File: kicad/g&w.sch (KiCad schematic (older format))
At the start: 181 parts, among them IC1 audio, IC2 MX25U8035F, IC3 vreg, IC4 pmic, IC5 BQ24072RGT_, J1 speaker, J2 SWD PORT, J3 DISPLAY1, J4 DISPLAY2, J5 Battery, J6 USB-C, Q1 PMBT3904, Q2 PMBT3904, Q3 PMBT3904, Q4 SSM6J412TU, Y1 H01717

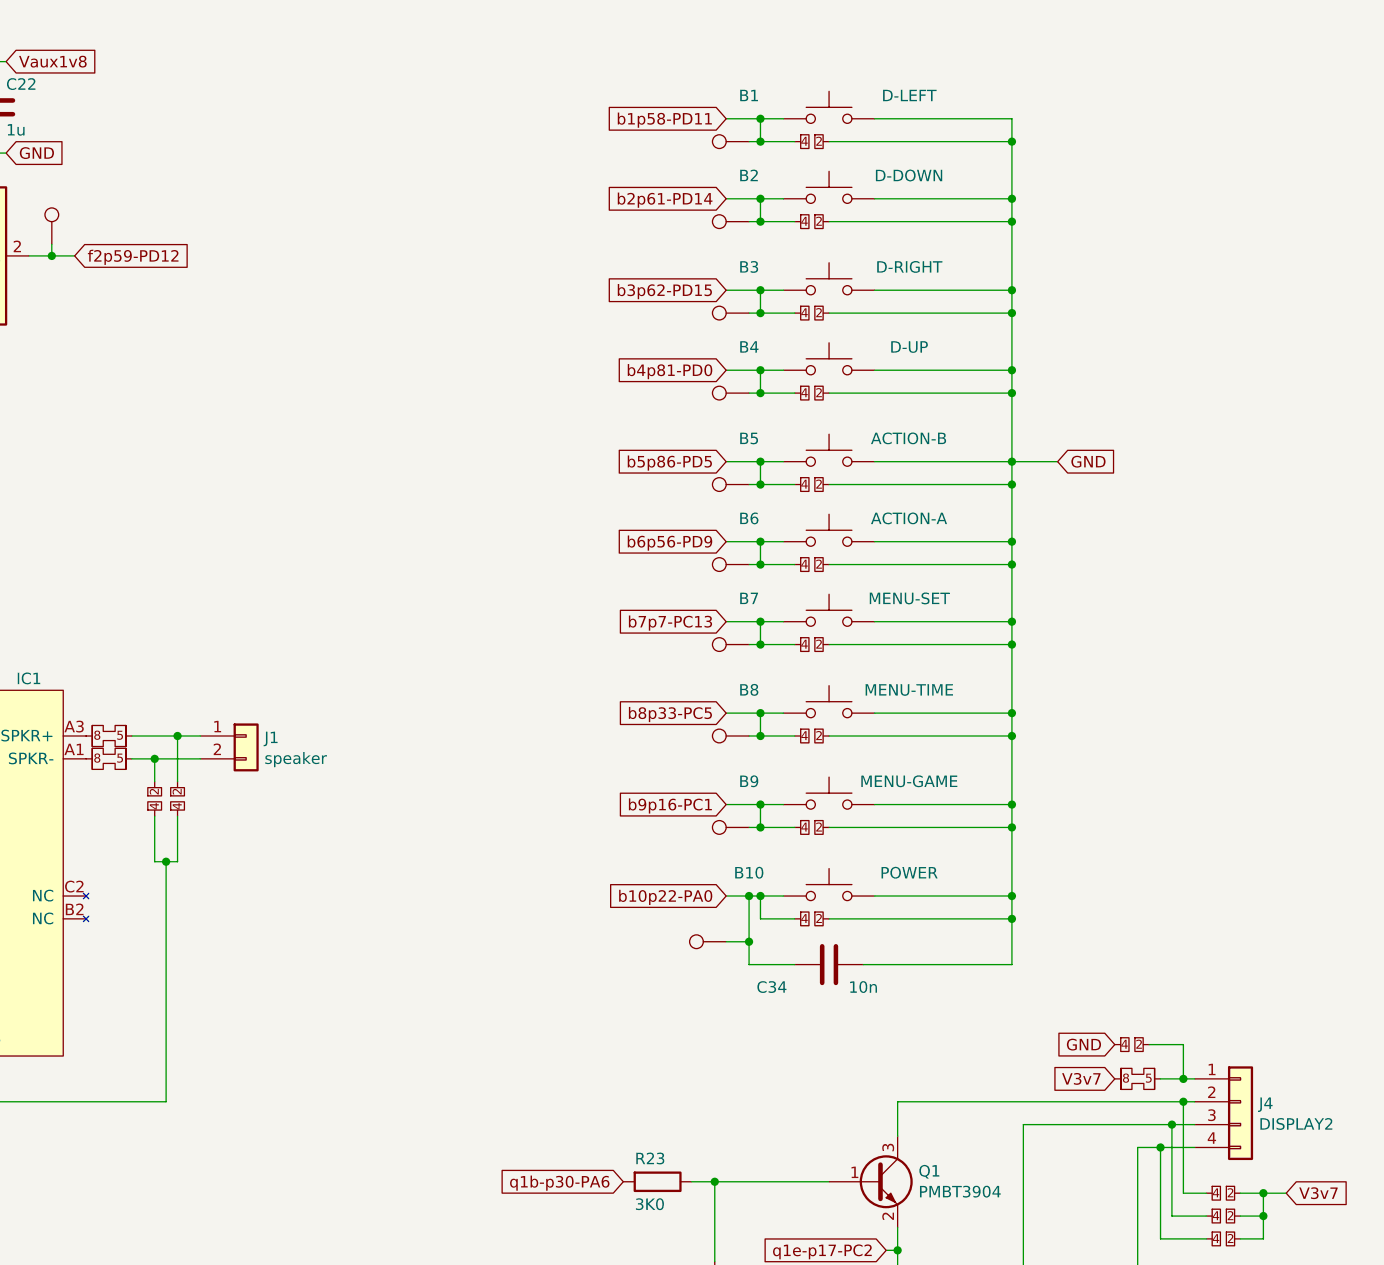
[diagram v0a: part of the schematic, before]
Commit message: kicad board outline
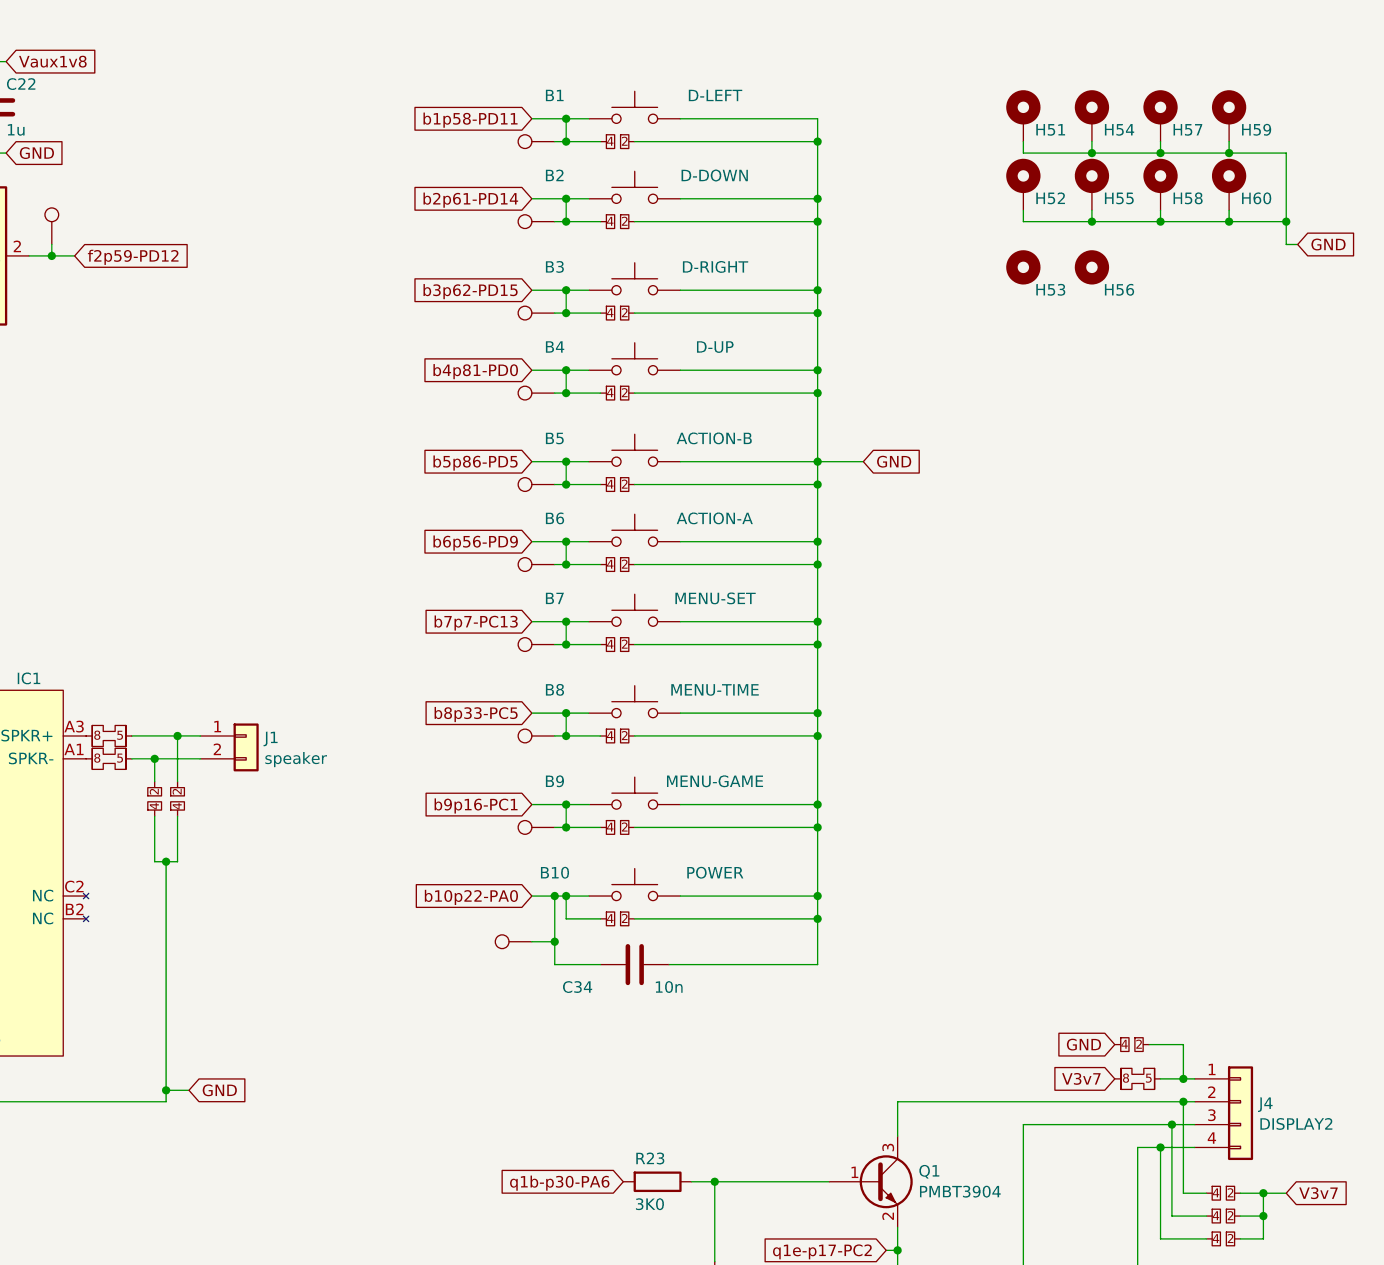
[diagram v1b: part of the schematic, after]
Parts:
- added H51, H52, H54, H55, H57, H58, H59, H60: MountingHole_Pad, gnw:MountingHole_2.0mm, symbol Mechanical:MountingHole_Pad
- added H53: MountingHole, gnw:MountingSlot_NC_1.3x2.2mm, symbol Mechanical:MountingHole
- added H56: MountingHole, gnw:MountingHole_NC_1.5mm, symbol Mechanical:MountingHole
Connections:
- net GND: now also IC1.A2 (GND), IC1.C3 (GND), JP78.1, JP79.1, JP86.1, JP87.1, R1.1, R2.2, R3.1, R4.2, H51.1, H52.1, H54.1, H55.1, H57.1, H58.1, H59.1, H60.1
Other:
- moved on the sheet: B1, B10, B2, B3, B4, B5, B6, B7, B8, B9, C34

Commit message: tweak footprints, setup design rules for 4 layers at common proto board house and refine board outline
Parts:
- TP51, TP52, TP53, TP54, TP55, TP56, TP57, TP58, TP59, TP60, TP61, TP62, TP63, TP64, TP65, TP66, TP67, TP68, TP69, TP70, TP71, TP72, TP73, TP74, TP75, TP76, TP77, TP78, TP79, TP80: footprint TestPoint:TestPoint_Pad_D1.0mm -> gnw:gnw-TestPoint_Pad_D1.0mm
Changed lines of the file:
@@
 F 0 "TP70" H 11158 7072 50  0001 L CNN
 F 1 "TestPoint" H 11158 7027 50  0001 L CNN
-F 2 "TestPoint:TestPoint_Pad_D1.0mm" H 11300 7000 50  0001 C CNN
+F 2 "gnw:gnw-TestPoint_Pad_D1.0mm" H 11300 7000 50  0001 C CNN
 F 3 "~" H 11300 7000 50  0001 C CNN
 	1    11100 7000
@@
 F 0 "TP68" H 9908 7722 50  0001 L CNN
 F 1 "TestPoint" H 9908 7677 50  0001 L CNN
-F 2 "TestPoint:TestPoint_Pad_D1.0mm" H 10050 7650 50  0001 C CNN
+F 2 "gnw:gnw-TestPoint_Pad_D1.0mm" H 10050 7650 50  0001 C CNN
 F 3 "~" H 10050 7650 50  0001 C CNN
 	1    9850 7650
@@
 F 0 "TP67" H 10158 1572 50  0001 L CNN
 F 1 "TestPoint" H 10158 1527 50  0001 L CNN
-F 2 "TestPoint:TestPoint_Pad_D1.0mm" H 10300 1500 50  0001 C CNN
+F 2 "gnw:gnw-TestPoint_Pad_D1.0mm" H 10300 1500 50  0001 C CNN
 F 3 "~" H 10300 1500 50  0001 C CNN
 	1    10100 1500
@@
 F 0 "TP63" H 8958 1472 50  0001 L CNN
 F 1 "TestPoint" H 8958 1427 50  0001 L CNN
-F 2 "TestPoint:TestPoint_Pad_D1.0mm" H 9100 1400 50  0001 C CNN
+F 2 "gnw:gnw-TestPoint_Pad_D1.0mm" H 9100 1400 50  0001 C CNN
 F 3 "~" H 9100 1400 50  0001 C CNN
 	1    8900 1400
@@
 F 0 "TP64" H 8958 1572 50  0001 L CNN
 F 1 "TestPoint" H 8958 1527 50  0001 L CNN
-F 2 "TestPoint:TestPoint_Pad_D1.0mm" H 9100 1500 50  0001 C CNN
+F 2 "gnw:gnw-TestPoint_Pad_D1.0mm" H 9100 1500 50  0001 C CNN
 F 3 "~" H 9100 1500 50  0001 C CNN
 	1    8900 1500
@@
 F 0 "TP65" H 8958 1672 50  0001 L CNN
 F 1 "TestPoint" H 8958 1627 50  0001 L CNN
-F 2 "TestPoint:TestPoint_Pad_D1.0mm" H 9100 1600 50  0001 C CNN
+F 2 "gnw:gnw-TestPoint_Pad_D1.0mm" H 9100 1600 50  0001 C CNN
 F 3 "~" H 9100 1600 50  0001 C CNN
 	1    8900 1600
@@
 F 0 "TP62" H 8958 1372 50  0001 L CNN
 F 1 "TestPoint" H 8958 1327 50  0001 L CNN
-F 2 "TestPoint:TestPoint_Pad_D1.0mm" H 9100 1300 50  0001 C CNN
+F 2 "gnw:gnw-TestPoint_Pad_D1.0mm" H 9100 1300 50  0001 C CNN
 F 3 "~" H 9100 1300 50  0001 C CNN
 	1    8900 1300
@@
 F 0 "TP66" H 8958 1772 50  0001 L CNN
 F 1 "TestPoint" H 8958 1727 50  0001 L CNN
-F 2 "TestPoint:TestPoint_Pad_D1.0mm" H 9100 1700 50  0001 C CNN
+F 2 "gnw:gnw-TestPoint_Pad_D1.0mm" H 9100 1700 50  0001 C CNN
 F 3 "~" H 9100 1700 50  0001 C CNN
 	1    8900 1700
@@
 F 0 "TP61" H 8158 9972 50  0001 L CNN
 F 1 "TestPoint" H 8158 9927 50  0001 L CNN
-F 2 "TestPoint:TestPoint_Pad_D1.0mm" H 8300 9900 50  0001 C CNN
+F 2 "gnw:gnw-TestPoint_Pad_D1.0mm" H 8300 9900 50  0001 C CNN
 F 3 "~" H 8300 9900 50  0001 C CNN
 	1    8100 9900
@@
 F 0 "TP56" H 4208 3372 50  0001 L CNN
 F 1 "TestPoint" H 4208 3327 50  0001 L CNN
-F 2 "TestPoint:TestPoint_Pad_D1.0mm" H 4350 3300 50  0001 C CNN
+F 2 "gnw:gnw-TestPoint_Pad_D1.0mm" H 4350 3300 50  0001 C CNN
 F 3 "~" H 4350 3300 50  0001 C CNN
 	1    4150 3300
@@
 F 0 "TP51" H 1358 6622 50  0001 L CNN
 F 1 "TestPoint" H 1358 6577 50  0001 L CNN
-F 2 "TestPoint:TestPoint_Pad_D1.0mm" H 1500 6550 50  0001 C CNN
+F 2 "gnw:gnw-TestPoint_Pad_D1.0mm" H 1500 6550 50  0001 C CNN
 F 3 "~" H 1500 6550 50  0001 C CNN
 	1    1300 6550
@@
 F 0 "TP55" H 3058 6372 50  0001 L CNN
 F 1 "TestPoint" H 3058 6327 50  0001 L CNN
-F 2 "TestPoint:TestPoint_Pad_D1.0mm" H 3200 6300 50  0001 C CNN
+F 2 "gnw:gnw-TestPoint_Pad_D1.0mm" H 3200 6300 50  0001 C CNN
 F 3 "~" H 3200 6300 50  0001 C CNN
 	1    3000 6300
@@
 F 0 "TP52" H 1558 7772 50  0001 L CNN
 F 1 "TestPoint" H 1558 7727 50  0001 L CNN
-F 2 "TestPoint:TestPoint_Pad_D1.0mm" H 1700 7700 50  0001 C CNN
+F 2 "gnw:gnw-TestPoint_Pad_D1.0mm" H 1700 7700 50  0001 C CNN
 F 3 "~" H 1700 7700 50  0001 C CNN
 	1    1500 7700
@@
 F 0 "TP54" H 2358 7772 50  0001 L CNN
 F 1 "TestPoint" H 2358 7727 50  0001 L CNN
-F 2 "TestPoint:TestPoint_Pad_D1.0mm" H 2500 7700 50  0001 C CNN
+F 2 "gnw:gnw-TestPoint_Pad_D1.0mm" H 2500 7700 50  0001 C CNN
 F 3 "~" H 2500 7700 50  0001 C CNN
 	1    2300 7700
@@
 F 0 "TP53" H 1958 10822 50  0001 L CNN
 F 1 "TestPoint" H 1958 10777 50  0001 L CNN
-F 2 "TestPoint:TestPoint_Pad_D1.0mm" H 2100 10750 50  0001 C CNN
+F 2 "gnw:gnw-TestPoint_Pad_D1.0mm" H 2100 10750 50  0001 C CNN
 F 3 "~" H 2100 10750 50  0001 C CNN
 	1    1900 10750
@@
 F 0 "TP72" H 12358 1122 50  0001 L CNN
 F 1 "TestPoint" H 12358 1077 50  0001 L CNN
-F 2 "TestPoint:TestPoint_Pad_D1.0mm" H 12500 1050 50  0001 C CNN
+F 2 "gnw:gnw-TestPoint_Pad_D1.0mm" H 12500 1050 50  0001 C CNN
 F 3 "~" H 12500 1050 50  0001 C CNN
 	1    12300 1050
@@
 F 0 "TP73" H 12358 1472 50  0001 L CNN
 F 1 "TestPoint" H 12358 1427 50  0001 L CNN
-F 2 "TestPoint:TestPoint_Pad_D1.0mm" H 12500 1400 50  0001 C CNN
+F 2 "gnw:gnw-TestPoint_Pad_D1.0mm" H 12500 1400 50  0001 C CNN
 F 3 "~" H 12500 1400 50  0001 C CNN
 	1    12300 1400
@@
 F 0 "TP74" H 12358 1872 50  0001 L CNN
 F 1 "TestPoint" H 12358 1827 50  0001 L CNN
-F 2 "TestPoint:TestPoint_Pad_D1.0mm" H 12500 1800 50  0001 C CNN
+F 2 "gnw:gnw-TestPoint_Pad_D1.0mm" H 12500 1800 50  0001 C CNN
 F 3 "~" H 12500 1800 50  0001 C CNN
 	1    12300 1800
@@
 F 0 "TP75" H 12358 2222 50  0001 L CNN
 F 1 "TestPoint" H 12358 2177 50  0001 L CNN
-F 2 "TestPoint:TestPoint_Pad_D1.0mm" H 12500 2150 50  0001 C CNN
+F 2 "gnw:gnw-TestPoint_Pad_D1.0mm" H 12500 2150 50  0001 C CNN
 F 3 "~" H 12500 2150 50  0001 C CNN
 	1    12300 2150
@@
 F 0 "TP76" H 12358 2622 50  0001 L CNN
 F 1 "TestPoint" H 12358 2577 50  0001 L CNN
-F 2 "TestPoint:TestPoint_Pad_D1.0mm" H 12500 2550 50  0001 C CNN
+F 2 "gnw:gnw-TestPoint_Pad_D1.0mm" H 12500 2550 50  0001 C CNN
 F 3 "~" H 12500 2550 50  0001 C CNN
 	1    12300 2550
@@
 F 0 "TP77" H 12358 2972 50  0001 L CNN
 F 1 "TestPoint" H 12358 2927 50  0001 L CNN
-F 2 "TestPoint:TestPoint_Pad_D1.0mm" H 12500 2900 50  0001 C CNN
+F 2 "gnw:gnw-TestPoint_Pad_D1.0mm" H 12500 2900 50  0001 C CNN
 F 3 "~" H 12500 2900 50  0001 C CNN
 	1    12300 2900
@@
 F 0 "TP78" H 12358 3322 50  0001 L CNN
 F 1 "TestPoint" H 12358 3277 50  0001 L CNN
-F 2 "TestPoint:TestPoint_Pad_D1.0mm" H 12500 3250 50  0001 C CNN
+F 2 "gnw:gnw-TestPoint_Pad_D1.0mm" H 12500 3250 50  0001 C CNN
 F 3 "~" H 12500 3250 50  0001 C CNN
 	1    12300 3250
@@
 F 0 "TP79" H 12358 3722 50  0001 L CNN
 F 1 "TestPoint" H 12358 3677 50  0001 L CNN
-F 2 "TestPoint:TestPoint_Pad_D1.0mm" H 12500 3650 50  0001 C CNN
+F 2 "gnw:gnw-TestPoint_Pad_D1.0mm" H 12500 3650 50  0001 C CNN
 F 3 "~" H 12500 3650 50  0001 C CNN
 	1    12300 3650
@@
 F 0 "TP80" H 12358 4122 50  0001 L CNN
 F 1 "TestPoint" H 12358 4077 50  0001 L CNN
-F 2 "TestPoint:TestPoint_Pad_D1.0mm" H 12500 4050 50  0001 C CNN
+F 2 "gnw:gnw-TestPoint_Pad_D1.0mm" H 12500 4050 50  0001 C CNN
 F 3 "~" H 12500 4050 50  0001 C CNN
 	1    12300 4050
@@
 F 0 "TP71" H 12258 4622 50  0001 L CNN
 F 1 "TestPoint" H 12258 4577 50  0001 L CNN
-F 2 "TestPoint:TestPoint_Pad_D1.0mm" H 12400 4550 50  0001 C CNN
+F 2 "gnw:gnw-TestPoint_Pad_D1.0mm" H 12400 4550 50  0001 C CNN
 F 3 "~" H 12400 4550 50  0001 C CNN
 	1    12200 4550
@@
 F 0 "TP69" H 10608 9572 50  0001 L CNN
 F 1 "TestPoint" H 10608 9527 50  0001 L CNN
-F 2 "TestPoint:TestPoint_Pad_D1.0mm" H 10750 9500 50  0001 C CNN
+F 2 "gnw:gnw-TestPoint_Pad_D1.0mm" H 10750 9500 50  0001 C CNN
 F 3 "~" H 10750 9500 50  0001 C CNN
 	1    10550 9500
@@
 F 0 "TP57" H 8258 4572 50  0001 L CNN
 F 1 "TestPoint" H 8258 4527 50  0001 L CNN
-F 2 "TestPoint:TestPoint_Pad_D1.0mm" H 8400 4500 50  0001 C CNN
+F 2 "gnw:gnw-TestPoint_Pad_D1.0mm" H 8400 4500 50  0001 C CNN
 F 3 "~" H 8400 4500 50  0001 C CNN
 	1    8200 4500
@@
 F 0 "TP58" H 8258 3822 50  0001 L CNN
 F 1 "TestPoint" H 8258 3777 50  0001 L CNN
-F 2 "TestPoint:TestPoint_Pad_D1.0mm" H 8400 3750 50  0001 C CNN
+F 2 "gnw:gnw-TestPoint_Pad_D1.0mm" H 8400 3750 50  0001 C CNN
 F 3 "~" H 8400 3750 50  0001 C CNN
 	1    8200 3750
@@
 F 0 "TP59" H 8258 4122 50  0001 L CNN
 F 1 "TestPoint" H 8258 4077 50  0001 L CNN
-F 2 "TestPoint:TestPoint_Pad_D1.0mm" H 8400 4050 50  0001 C CNN
+F 2 "gnw:gnw-TestPoint_Pad_D1.0mm" H 8400 4050 50  0001 C CNN
 F 3 "~" H 8400 4050 50  0001 C CNN
 	1    8200 4050
@@
 F 0 "TP60" H 8258 3522 50  0001 L CNN
 F 1 "TestPoint" H 8258 3477 50  0001 L CNN
-F 2 "TestPoint:TestPoint_Pad_D1.0mm" H 8400 3450 50  0001 C CNN
+F 2 "gnw:gnw-TestPoint_Pad_D1.0mm" H 8400 3450 50  0001 C CNN
 F 3 "~" H 8400 3450 50  0001 C CNN
 	1    8200 3450

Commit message: wanted
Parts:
- IC2: value MX25U8035F -> MX25U8035FM2
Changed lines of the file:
@@
 P 9500 1550
 F 0 "IC2" H 9100 1200 50  0000 L CNN
-F 1 "MX25U8035F" H 9100 1900 50  0000 L CNN
+F 1 "MX25U8035FM2" H 9050 1900 50  0000 L CNN
 F 2 "Package_SO:SOP-8_5.28x5.23mm_P1.27mm" H 9500 950 50  0001 C CNN
 F 3 "http://www.macronix.com/Lists/Datasheet/Attachments/7534/MX25R3235F,%20Wide%20Range,%2032Mb,%20v1.6.pdf" H 9500 1550 50  0001 C CNN
